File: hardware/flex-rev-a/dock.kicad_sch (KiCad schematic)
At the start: 0 parts

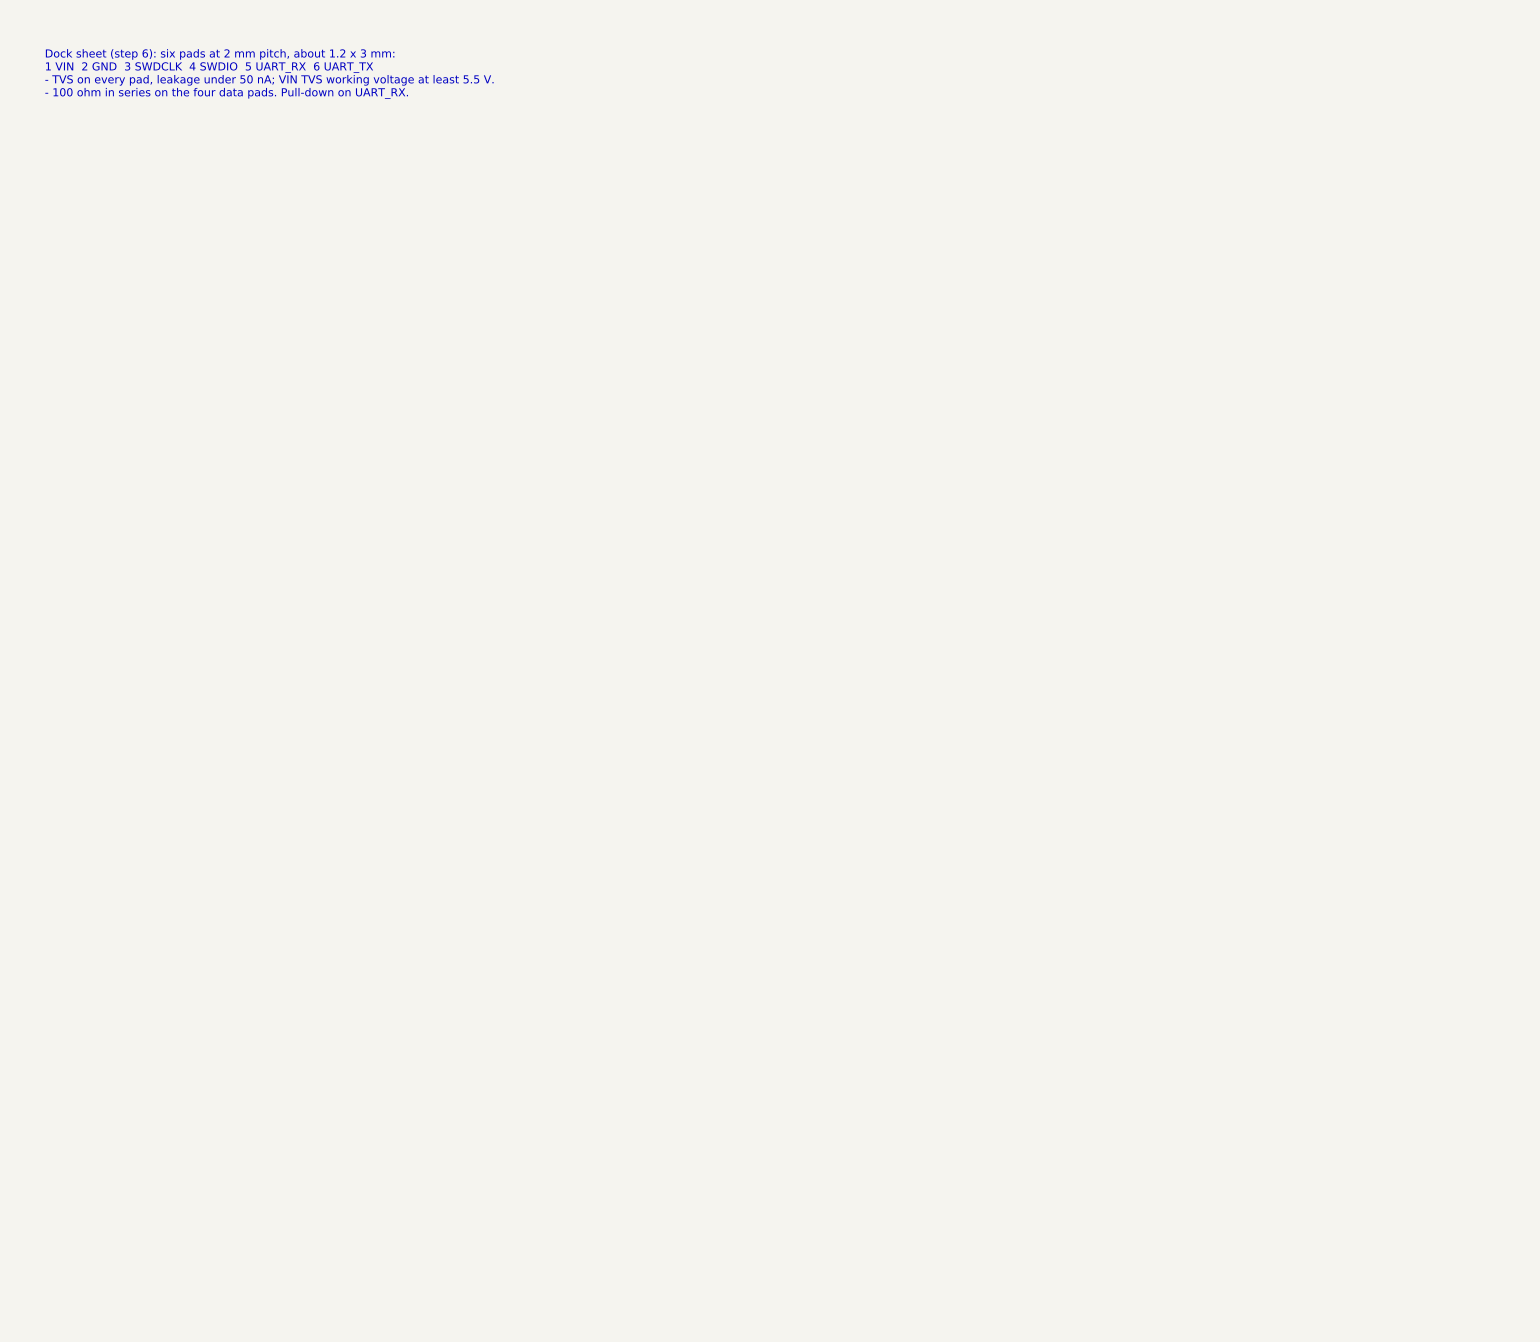
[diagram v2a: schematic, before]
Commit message: Draw dock sheet: six pogo pads with TVS and series resistors
- J601: six pads at 2 mm pitch, 1.2 x 3.0 mm (project footprint), order
  VIN, GND, SWDCLK, SWDIO, UART_RX, UART_TX.
- TPD1E10B06 TVS at the VIN pad and each data pad (D601-D605); none on
  the GND pad.
- 100 ohm in series between each data pad and the SoC net; 100k
  pull-down on UART_RX at the SoC side.
- VIN TVS and its PWR_FLAG move from the power sheet to the pad (the pads
  and the PMIC sit on different flex islands).
- (check) TPD1E10B06 leakage is 100 nA max at 5 V, above the 50 nA target;
  no 1.8 V figure for the data pads.

ERC: 1 error (nRESET, debug sheet next), 3 warnings; SWDCLK error cleared.

Co-Authored-By: Claude Opus 5.5 <noreply@anthropic.com>
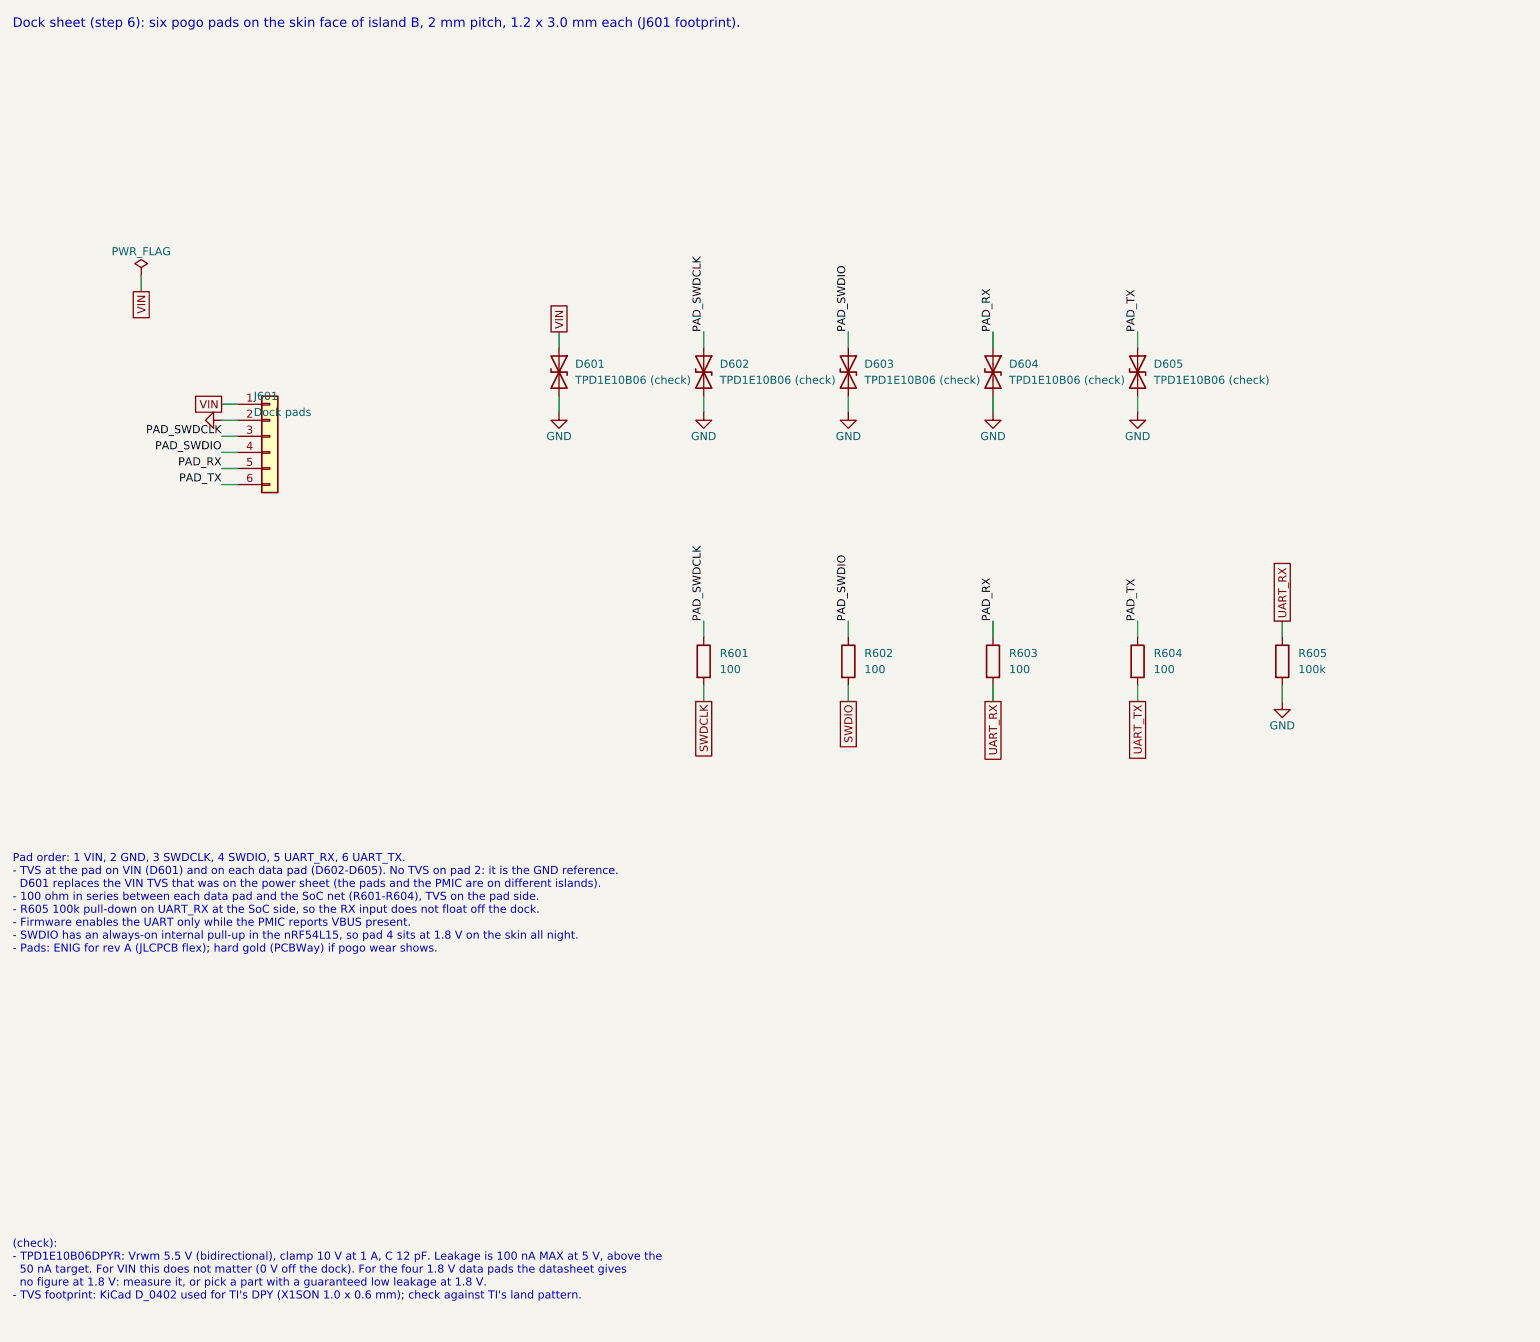
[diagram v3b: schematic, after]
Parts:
- added D601, D602, D603, D604, D605: TPD1E10B06 (check), Diode_SMD:D_0402_1005Metric, symbol Device:D_TVS
- added J601: Dock pads, wakeband:DockPads_1x06_P2.0mm_1.2x3.0mm, symbol Connector_Generic:Conn_01x06
- added R601, R602, R603, R604: 100, Resistor_SMD:R_0402_1005Metric, symbol Device:R
- added R605: 100k, Resistor_SMD:R_0402_1005Metric, symbol Device:R
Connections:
- new net GND: D601.2 (A2), D602.2 (A2), D603.2 (A2), D604.2 (A2), D605.2 (A2), J601.2 (Pin_2), R605.2
- new net PAD_RX: D604.1 (A1), J601.5 (Pin_5), R603.1
- new net PAD_SWDCLK: D602.1 (A1), J601.3 (Pin_3), R601.1
- new net PAD_SWDIO: D603.1 (A1), J601.4 (Pin_4), R602.1
- new net PAD_TX: D605.1 (A1), J601.6 (Pin_6), R604.1
- new net SWDCLK: R601.2
- new net SWDIO: R602.2
- new net UART_RX: R603.2, R605.1
- new net UART_TX: R604.2
- new net VIN: D601.1 (A1), J601.1 (Pin_1)
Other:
- note added: "(check): - TPD1E10B06DPYR: Vrwm 5.5 V (bidirectional), clamp 10 V at 1 A, C 12 pF. Leakage is 100 nA MAX at 5 V, above the 50 nA target. For VIN this does not matter (0 V off the dock). For the four 1.8 V data pads the datasheet gives no figure at 1.8 V: measure it, or pick a part with a guaranteed low leakage at 1.8 V. - TVS footprint: KiCad D_0402 used for TI's DPY (X1SON 1.0 x 0.6 mm); check a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"
- note added: "Dock sheet (step 6): six pogo pads on the skin face of island B, 2 mm pitch, 1.2 x 3.0 mm each (J601 footprint)."
- note added: "Pad order: 1 VIN, 2 GND, 3 SWDCLK, 4 SWDIO, 5 UART_RX, 6 UART_TX. - TVS at the pad on VIN (D601) and on each data pad (D602-D605). No TVS on pad 2: it is the GND reference. D601 replaces the VIN TVS that was on the power sheet (the pads and the PMIC are on different islands). - 100 ohm in series between each data pad and the SoC net (R601-R604), TVS on the pad side. - R605 100k pull-down on UART_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"
- note removed: "Dock sheet (step 6): six pads at 2 mm pitch, about 1.2 x 3 mm: 1 VIN 2 GND 3 SWDCLK 4 SWDIO 5 UART_RX 6 UART_TX - TVS on every pad, leakage under 50 nA; VIN TVS working voltage at least 5.5 V. - 100 ohm in series on the four data pads. Pull-down on UART_RX."

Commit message: Finish rev A schematic pass: clean ERC, BOM with LCSC numbers
- ERC 0 errors, 0 warnings: the ISP2454 symbol's ground pins renamed from
  VSS to GND (same pins), so they no longer clash with the GND label.
- Sensors: larger LIS2DW12 symbol so pin names and GND symbols no longer
  overlap. Dock: connector mirrored and TVS spacing widened for
  readability. No connectivity changes.
- bom.csv: JLCPCB-style columns with LCSC numbers checked on lcsc.com;
  ISP2454-LX and nPM1304-QEAA have none. Pads, jumper and net tie excluded.
- All 50 references annotated and unique; PDF replotted; README status
  table, ERC notes and plan progress updated.

Co-Authored-By: Claude Opus 5.5 <noreply@anthropic.com>
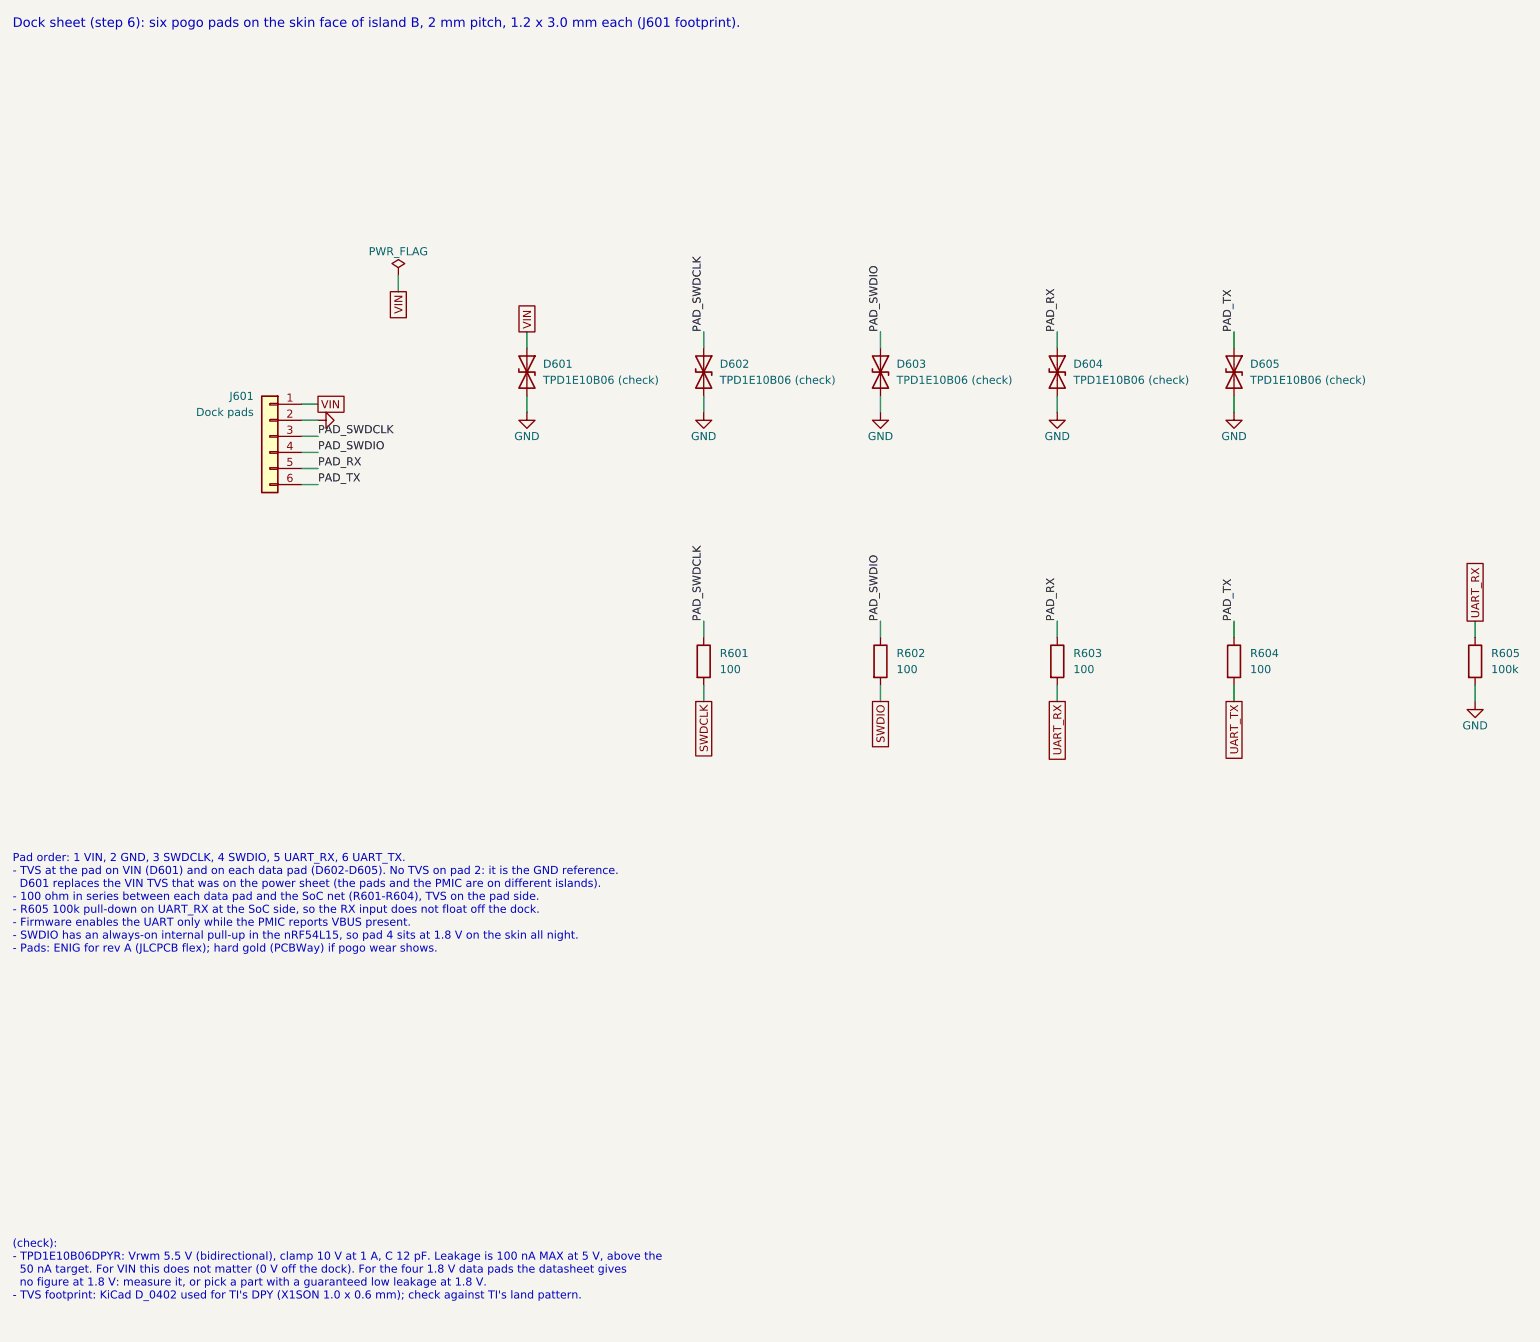
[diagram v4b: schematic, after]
